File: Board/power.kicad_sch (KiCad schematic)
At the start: 27 parts, among them U1 LMR51635XDDCR, U2 MP2459

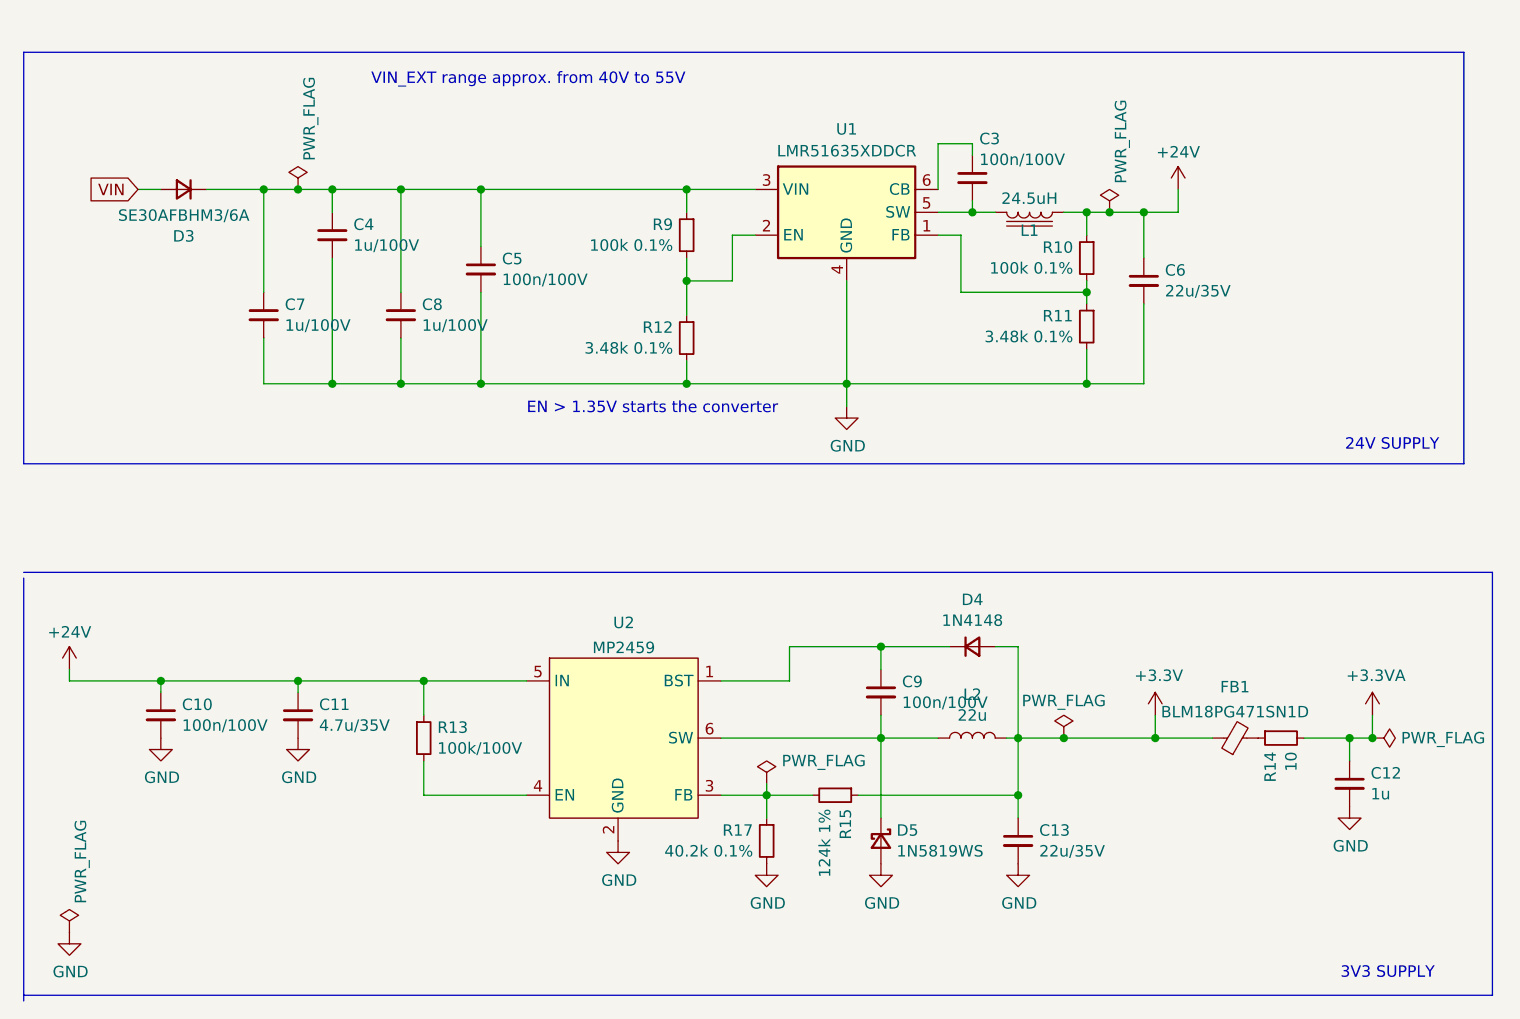
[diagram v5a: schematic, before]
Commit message: Routing done with polyfuse. Need to tidy silkscreen.
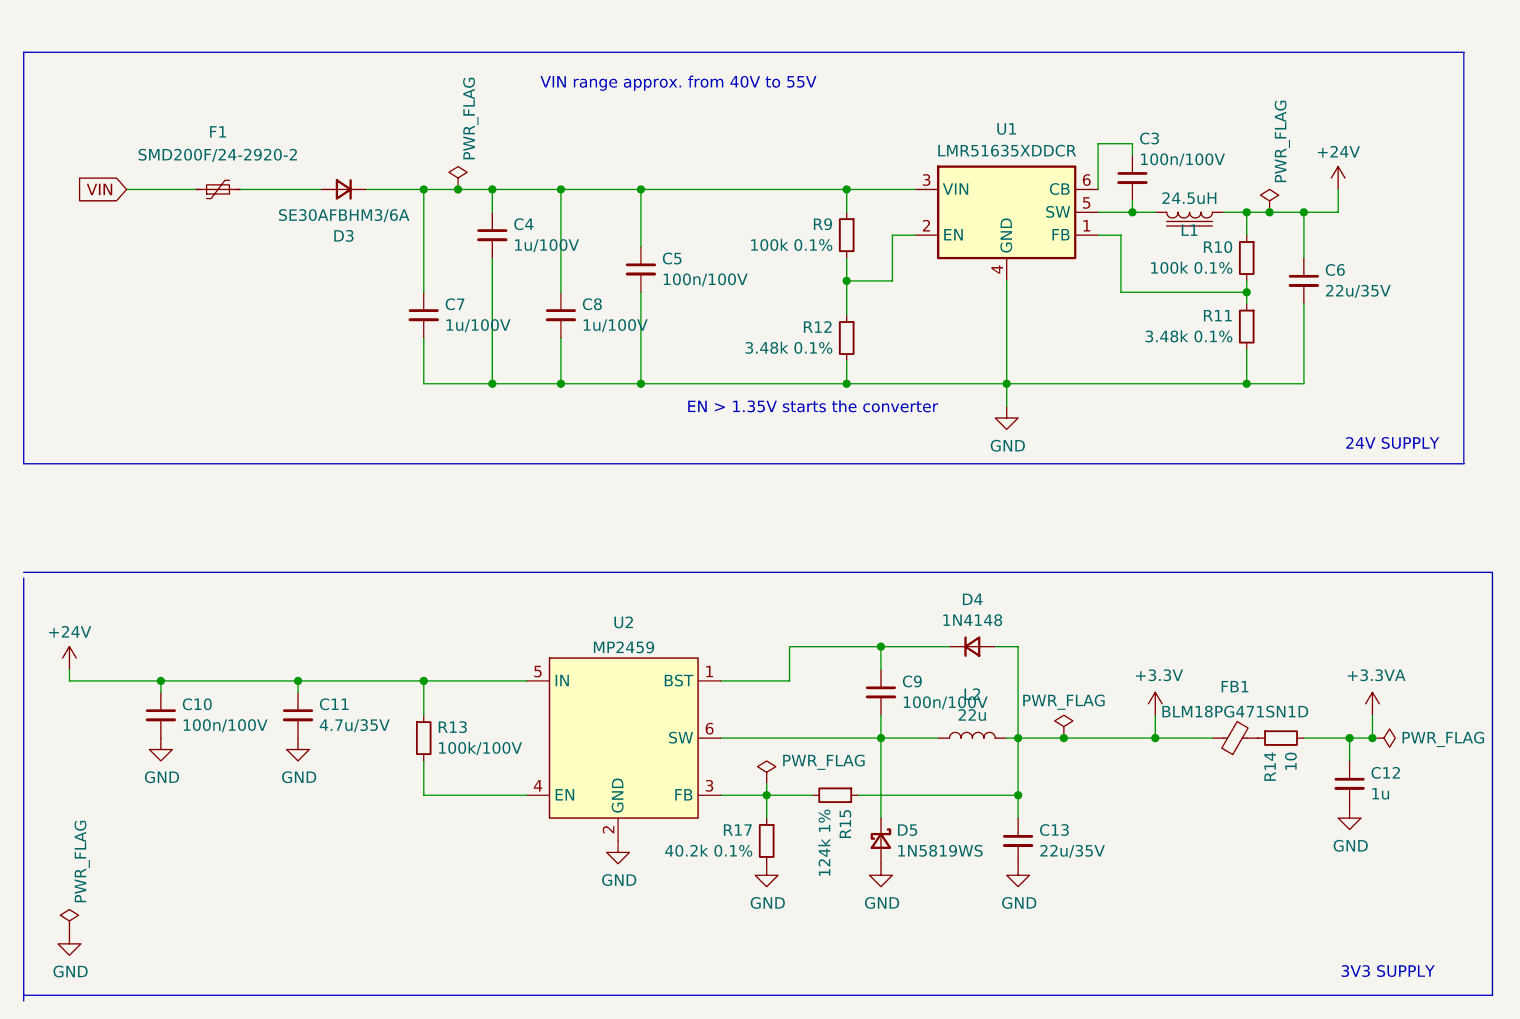
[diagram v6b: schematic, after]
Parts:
- added F1: SMD200F/24-2920-2, Fuse:Fuse_2920_7451Metric_Pad2.10x5.45mm_HandSolder, symbol Device:Polyfuse_Small
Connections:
- net VIN: now also F1.1; no longer D3.2 (A)
- new net: D3.2 (A), F1.2
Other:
- note added: "VIN range approx. from 40V to 55V"
- note removed: "VIN_EXT range approx. from 40V to 55V"
- moved on the sheet: C3, C4, C5, C6, C7, C8, D3, L1, R10, R11, R12, R9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

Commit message: Silkscreen done.
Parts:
- L1: symbol Device:L_Iron -> inductors_custom:L_Iron_3_pins
- renumbered C3 to C14, C5 to C15, C12 to C16, C4 to C18, C9 to C19, C7 to C20, C8 to C21, C11 to C25, C10 to C26, C13 to C27, C6 to C9, D4 to D2, FB1 to FB3, R12 to R10, R9 to R12, R17 to R13, R15 to R14, R14 to R16, R13 to R20, R11 to R8, R10 to R9, U1 to U2, U2 to U4
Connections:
- net GND: now also L1.3 (case)
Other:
- moved on the sheet: C9, R8

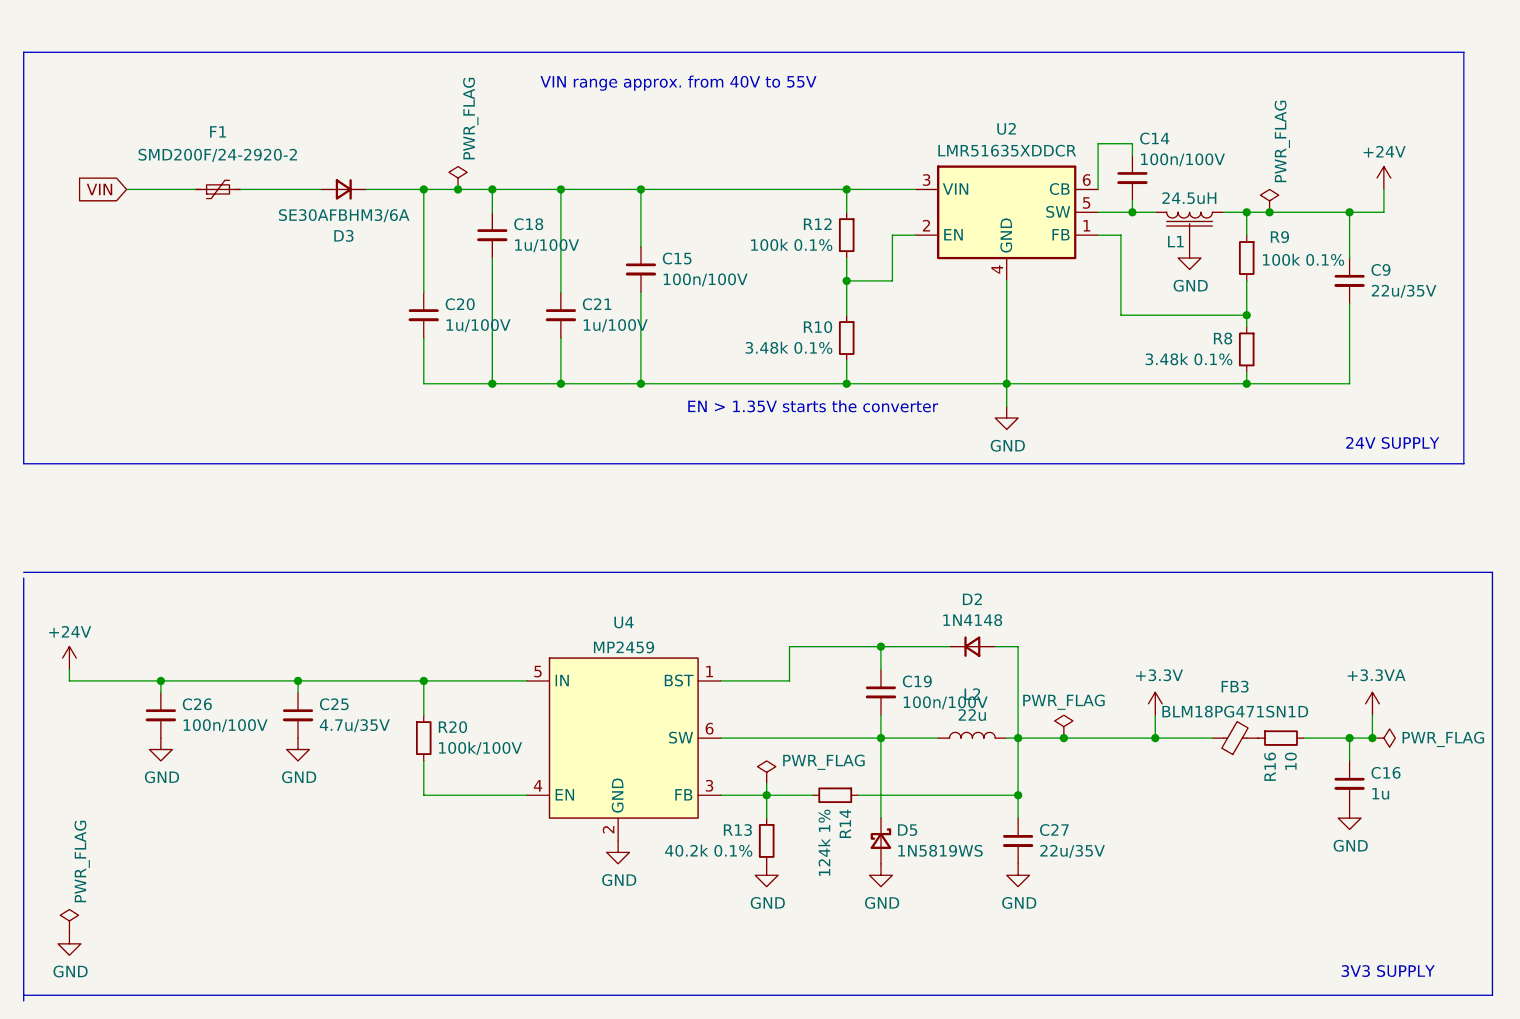
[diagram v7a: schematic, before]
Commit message: Changed some components based on availability.
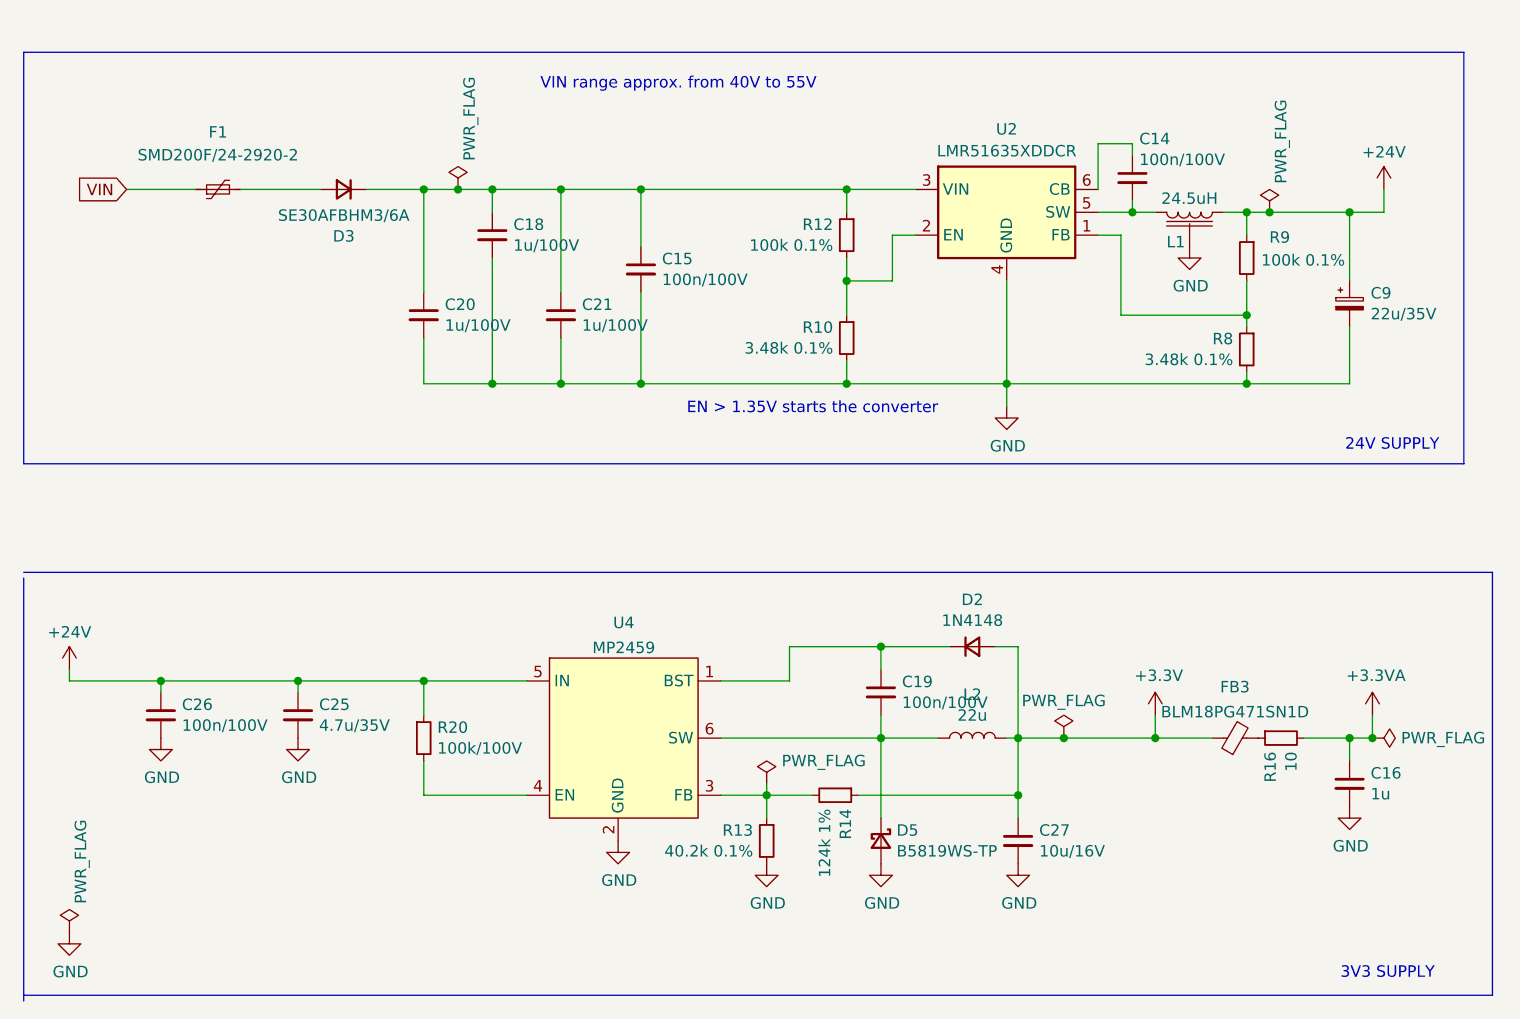
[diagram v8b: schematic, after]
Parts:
- C27: value 22u/35V -> 10u/16V
- C9: footprint Capacitor_SMD:C_0805_2012Metric_Pad1.18x1.45mm_HandSolder -> Capacitor_SMD:CP_Elec_6.3x5.8; symbol Device:C_Small -> Device:C_Polarized_Small; REF (none) -> EEH-ZA1V330P
- D5: value 1N5819WS -> B5819WS-TP; REF 1N5819WS -> B5819WS-TP
- FB3: footprint Inductor_SMD:L_0603_1608Metric -> Inductor_SMD:L_0603_1608Metric_Pad1.05x0.95mm_HandSolder
- L2: footprint Inductor_SMD:L_1008_2520Metric -> Inductor_SMD:L_1008_2520Metric_Pad1.43x2.20mm_HandSolder
